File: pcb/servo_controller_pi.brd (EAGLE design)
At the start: 56 parts, among them IC1 PIC18F452, IC2 LM2936MP-3.0, IC3 MAX4173FESA+, Q1 10Mhz

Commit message: Raspberry Pi
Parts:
- removed PW: TL36PO, switch:TL3XPO
- added C10, C11: (no value), rcl:C0805
- added C12: 10uf, rcl:C1206
- added C13: 100nf, rcl:C1206
- added D4: 3V3, diode:SOT23
- added D5: MBRA340T3, diode:SMA
- added GY-27: (no value), con-lstb:MA05-1
- added IC4: LM2936MP-3.3, national-semiconductor:SOT223
- added IC5: 4512D, 45xx:SO16
- added IN, OUT: (no value), con-wago-500:W237-102
- added LED-STRIP: (no value), con-lstb:MA04-1
- added Q2: BUZ10, transistor-fet:TO220
- added R8: (no value), rcl:M0805
- added RN1: (no value), resistor-sil:SIL9
- added SV1, SV2: (no value), con-lstb:MA08-1W
- D2: value 5v1 -> 3V3
- IC2: value LM2936MP-3.0 -> LM2936MP-5.0
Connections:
- removed net N$15: PW.2, X1.2
- new net +15V: IN.1, OUT.1
- new net +3V3: D5.C, U$3.1, U$3.17
- new net ADDRA: IC5.11
- new net ADDRB: IC5.12
- new net ADDRC: IC5.13
- new net CO: LED-STRIP.2
- new net DO: LED-STRIP.3
- new net N$26: IC5.6, RN1.7, SV2.6
- new net N$28: IC5.5, RN1.6, SV2.8
- new net N$29: IC5.4, RN1.5, SV1.2
- new net N$30: IC5.3, RN1.4, SV1.4
- new net N$31: IC5.2, RN1.3, SV1.6
- new net N$33: IC5.1, RN1.2, SV1.8
- new net N$34: IC5.7, RN1.8, SV2.4
- new net N$35: IC5.9, RN1.9, SV2.2
- new net N$36: OUT.2, Q2.2
- new net N$38: C12.1, D5.A, IC4.3
- new net OUT: D4.3, IC5.14
- new net POUT: Q2.1, R8.2
- new net SCL: GY-27.4
- new net SDA: GY-27.3
- net +5V: now also C10.1, C11.1, C13.1, GY-27.5, IC4.1, IC5.16, LED-STRIP.4, SV1.1, SV1.3, SV1.5, SV1.7, SV2.1, SV2.3, SV2.5, SV2.7, U$3.2, U$3.4
- net VDD: now also X1.2; no longer PW.1
- net VSS: now also C10.2, C11.2, C12.2, C13.2, D4.1, GY-27.1, IC4.2, IC4.4, IC5.10, IC5.15, IC5.8, IN.2, LED-STRIP.1, Q2.3, R8.1, RN1.1, U$3.14, U$3.20, U$3.25, U$3.6, U$3.9
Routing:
- net LED0: track 71.1 -> 0.00 mm, vias 1 -> 0
- net VSS: track 195.0 -> 142.9 mm
- net LED1: track 66.0 -> 15.2 mm, vias 2 -> 1
- net SWITCH0: track 72.0 -> 22.1 mm
- net SWITCH1: track 58.3 -> 10.2 mm
- net RX_FROM_ARDUINO: track 29.2 -> 0.27 mm
- net TX_FROM_ARDUINO: track 27.5 -> 0.00 mm
- net VDD: track 144.1 -> 134.6 mm
- net N$15: track 7.23 -> 0.00 mm
- net OPTION0: track 3.07 -> 0.00 mm
- net OPTION3: track 3.07 -> 0.00 mm

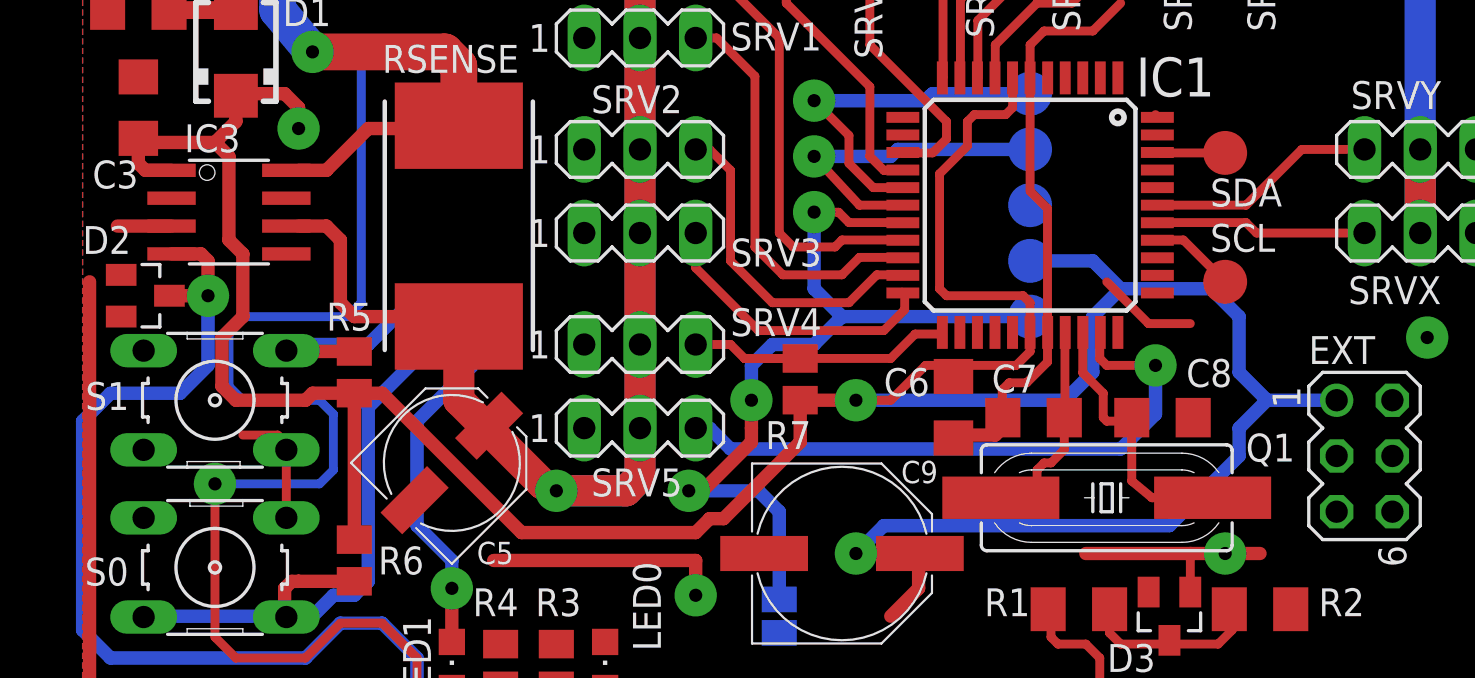
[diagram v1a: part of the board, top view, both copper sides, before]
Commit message: Raspberry Pi pcb version
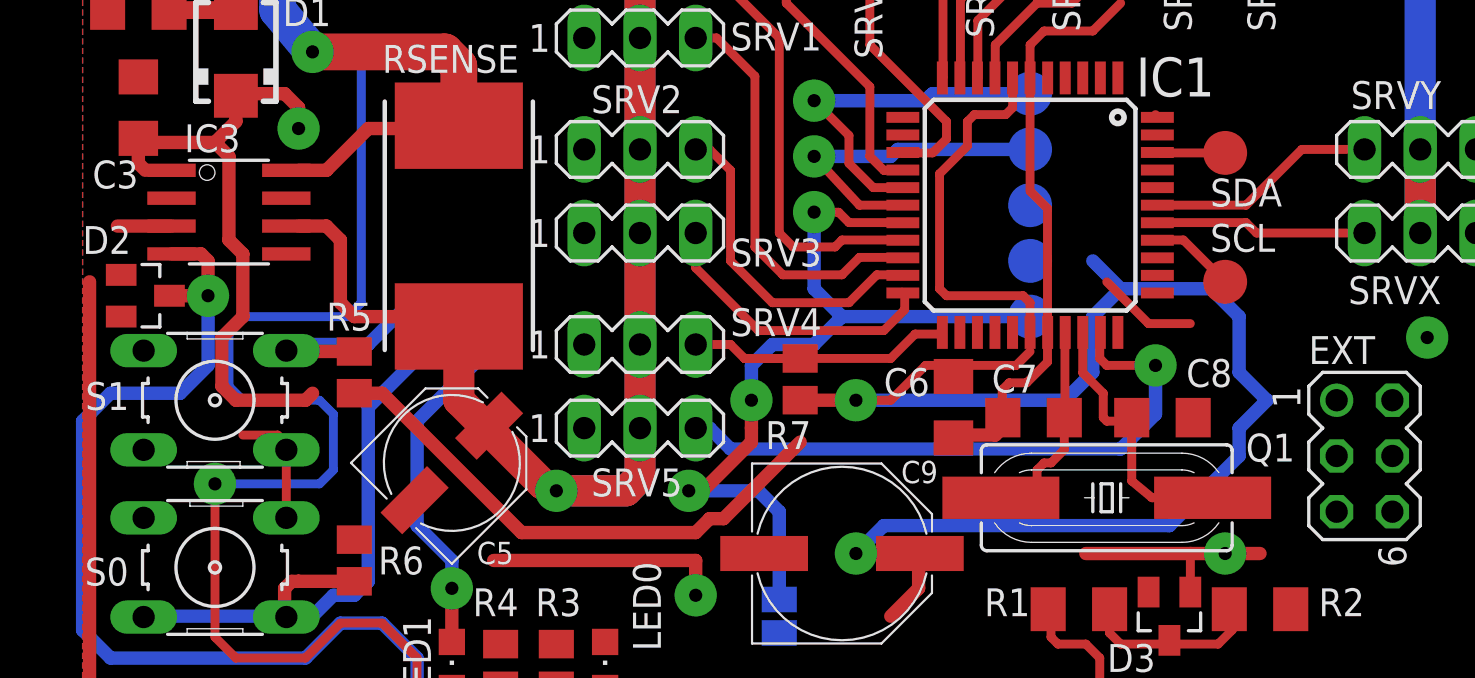
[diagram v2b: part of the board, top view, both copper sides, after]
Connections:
- net +3V3: now also C10.1, C11.1, C3.1, C6.1, EXT.1, GY-27.5, IC1.28, IC1.7, IC3.1, IC5.16, LED-STRIP.4, R5.2, R6.2, R7.2, SV1.1, SV1.3, SV1.5, SV1.7, SV2.1, SV2.3, SV2.5, SV2.7, VDD.TP; no longer U$3.17
- net +5V: no longer C10.1, C11.1, C3.1, C6.1, EXT.1, GY-27.5, IC1.28, IC1.7, IC3.1, IC5.16, LED-STRIP.4, R5.2, R6.2, R7.2, SV1.1, SV1.3, SV1.5, SV1.7, SV2.1, SV2.3, SV2.5, SV2.7, U$3.4, VDD.TP
- net LIPO_VOLTAGE: now also IC1.24
- net SERVO_CURRENT: now also IC1.25
- net VSS: no longer U$3.14, U$3.20, U$3.25, U$3.9
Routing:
- net +5V: track 160.0 -> 97.4 mm
- net +3V3: track 0.00 -> 42.9 mm

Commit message: Schema Pi
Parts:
- removed EXT: (no value), con-lstb:MA03-2
- moved D1 40.5 mm to (35.6, 61.0)
- moved IC2 26.4 mm to (26.7, 61.3)
- moved C1 19.2 mm to (16.8, 61.6)
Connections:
- removed net N$16: SJ1.2
- removed net OPTION0: EXT.3
- removed net OPTION1: EXT.5
- removed net OPTION2: EXT.6
- removed net OPTION3: EXT.4
- removed net RX_FROM_ARDUINO: IC1.44
- removed net SWITCH0: R6.1, S0.1
- removed net SWITCH1: R5.1, S1.2
- removed net TX_FROM_ARDUINO: IC1.1
- new net RX_PI: IC1.44, U$3.10
- new net SO: U$3.23
- new net SW0: R6.1, S0.1, U$3.16
- new net SW1: R5.1, S1.2, U$3.18
- new net TX_PI: IC1.1, U$3.8
- net +3V3: no longer EXT.1, LED-STRIP.4
- net +5V: now also LED-STRIP.4
- net ADDRA: now also U$3.22
- net ADDRB: now also U$3.24
- net ADDRC: now also U$3.26
- net DO: now also U$3.19
- net LED0: now also U$3.7
- net LED1: now also U$3.11
- net OUT: now also U$3.12
- net POUT: now also U$3.15
- net SCL: now also U$3.5
- net SDA: now also U$3.3
- net VSS: no longer EXT.2
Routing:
- net VDD: track 134.6 -> 58.9 mm, vias 2 -> 1
- net SERVO_CURRENT: track 80.9 -> 6.04 mm
- net +5V: track 97.4 -> 69.9 mm, vias 3 -> 2
- net SWITCH0: track 22.1 -> 0.00 mm
- net SW0: track 0.00 -> 22.1 mm
- net SWITCH1: track 10.2 -> 0.00 mm
- net SW1: track 0.00 -> 9.78 mm
- net N$20: track 9.11 -> 0.00 mm

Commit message: Raspberry Pi PCB
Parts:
- moved D2 93.7 mm to (87.9, 61.9)
- moved IC3 92.7 mm to (86.7, 72.7)
- moved C3 90.3 mm to (85.7, 66.7)
- moved RSENSE 88.1 mm to (95.2, 66.4)
- moved S0 72.8 mm to (56.2, 61.6)
- moved C9 72.3 mm to (72.7, 70.5)
- moved S1 71.9 mm to (55.6, 68.6)
- moved D3 69.2 mm to (37.5, 73.3)
- moved R6 69.0 mm to (57.5, 61.3)
- moved R5 68.9 mm to (58.1, 69.2)
- moved R1 68.1 mm to (32.7, 72.4)
- moved R2 67.9 mm to (42.2, 72.4)
- moved SJ1 66.8 mm to (22.9, 71.4)
- moved LED0 66.0 mm to (12.4, 67.9)
- moved LED1 66.0 mm to (5.40, 67.9)
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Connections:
- net UC_RESET: no longer SJ1.1
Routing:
- net VDD: track 58.9 -> 0.00 mm, vias 1 -> 0
- net +5V: track 69.9 -> 11.4 mm, vias 2 -> 0
- net N$6: track 28.1 -> 54.2 mm
- net +3V3: track 42.9 -> 17.6 mm
- net SW0: track 22.1 -> 0.00 mm
- net N$5: track 14.5 -> 35.0 mm
- net N$4: track 13.5 -> 28.9 mm
- net LED1: track 15.2 -> 0.00 mm, vias 1 -> 0
- net N$10: track 17.6 -> 32.5 mm
- net VEE: track 170.4 -> 155.9 mm, vias 1 -> 0
- net N$12: track 11.0 -> 25.1 mm
- net N$13: track 8.91 -> 22.9 mm
- net N$11: track 14.7 -> 28.7 mm
- net N$32: track 15.1 -> 26.3 mm
- net N$3: track 15.3 -> 26.2 mm
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
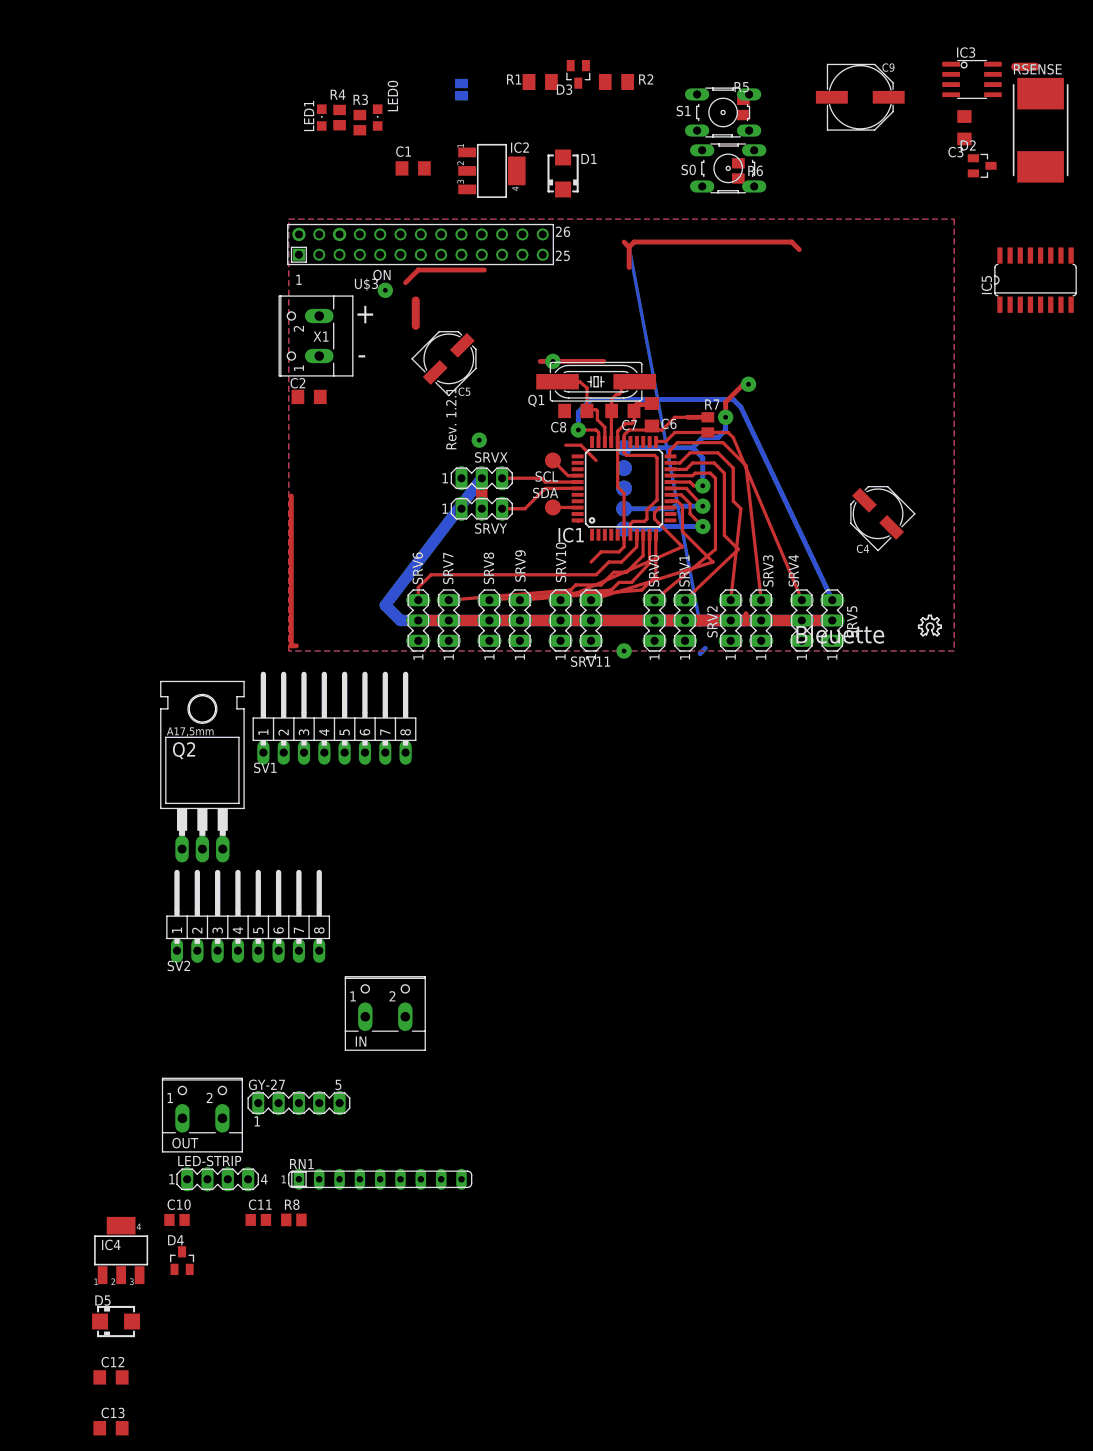
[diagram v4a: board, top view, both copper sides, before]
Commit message: Sensor board milling + Raspberry Pi update
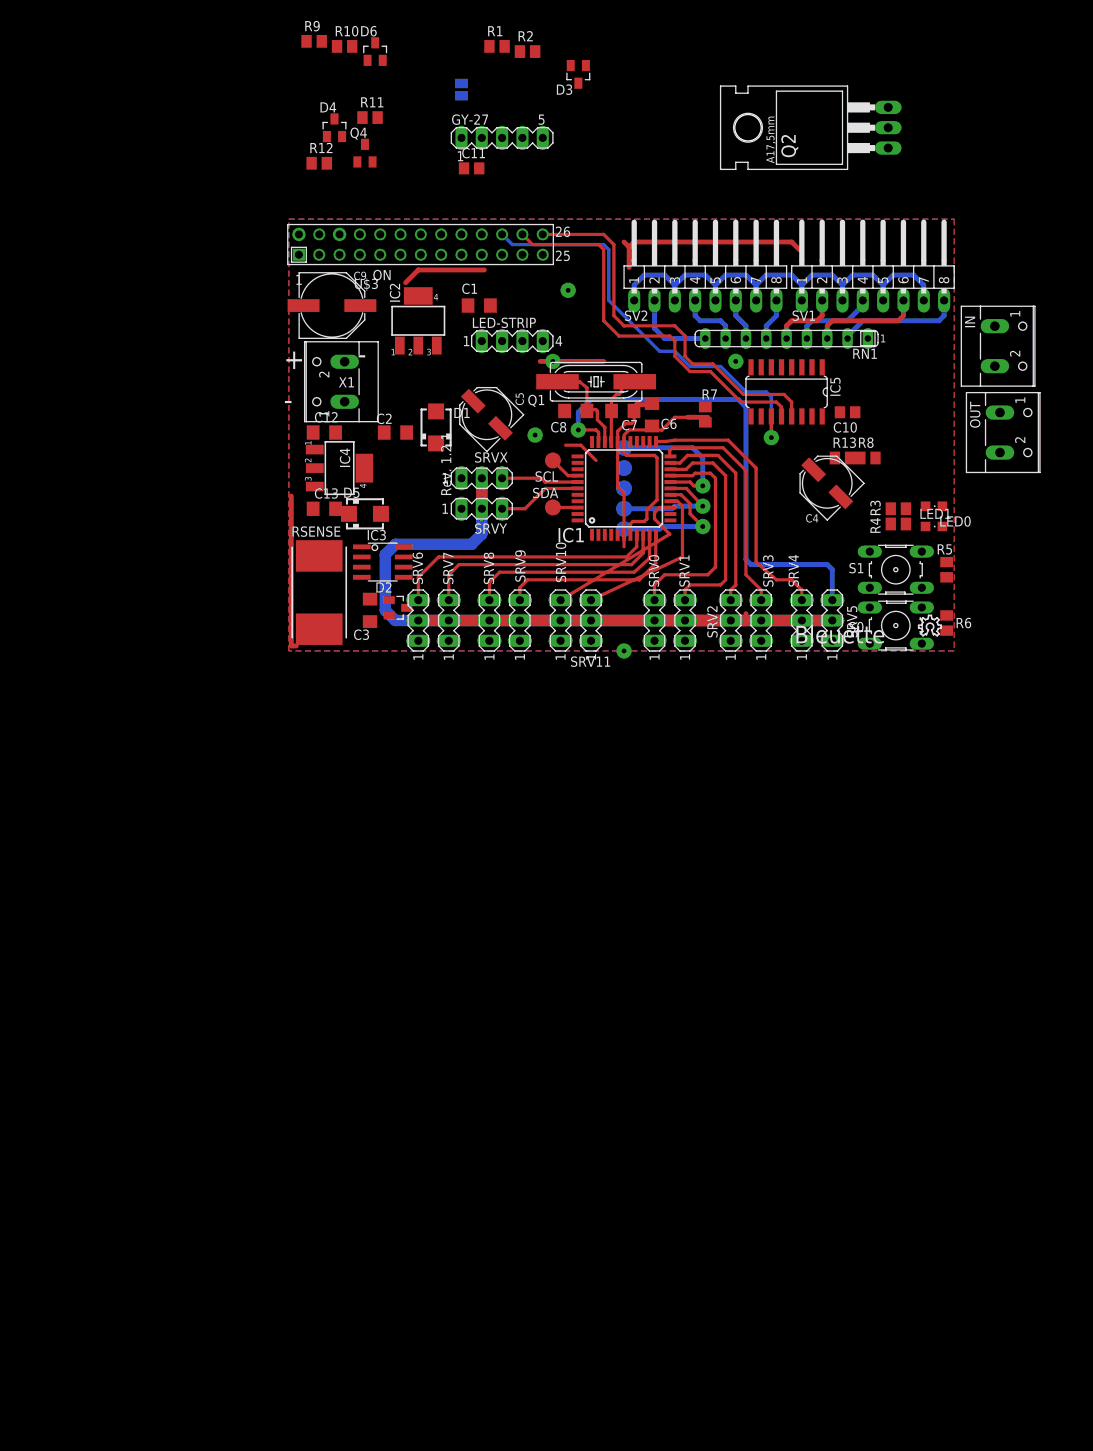
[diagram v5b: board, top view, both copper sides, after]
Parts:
- added D6: 3V3, diode:SOT23
- added Q4: BC848ALT1SMD, transistor-npn:SOT23
- added R10: 2k2, rcl:M0805
- added R11, R12, R13: 1k, rcl:M0805
- added R9: 3k3, rcl:M0805
- D2: value 3V3 -> 5V1
- R1, R2: device rcl:M1206 -> rcl:M0805
- moved D4 142.9 mm to (6.99, 66.7)
- moved C11 134.1 mm to (24.1, 61.6)
- moved OUT 131.6 mm to (91.4, 28.6), turned to 270 degrees
- moved C10 131.2 mm to (71.1, 31.1), turned to 180 degrees
- moved GY-27 123.3 mm to (27.9, 65.4)
- moved C12 121.1 mm to (5.71, 28.6)
- moved R8 119.3 mm to (73.7, 25.4)
- moved C13 118.0 mm to (5.71, 19.1)
- moved RN1 116.7 mm to (63.5, 40.3), turned to 180 degrees
- moved Q2 115.4 mm to (69.8, 66.7), turned to 90 degrees
- moved IN 113.2 mm to (90.8, 39.4), turned to 270 degrees
- moved LED-STRIP 111.1 mm to (29.2, 40.0)
- moved RSENSE 107.1 mm to (5.08, 8.57)
- moved D5 105.7 mm to (10.8, 18.4)
- moved IC4 101.5 mm to (7.62, 24.1), turned to 270 degrees
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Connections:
- new net N$15: IC1.1, Q4.2, R11.1
- new net N$16: IC1.44, R10.2
- new net N$21: D4.3, Q4.1, R12.1
- new net N$37: IC5.14, R13.2
- net +3V3: no longer C3.1, C6.1, IC1.28, IC1.7, IC3.1, R7.2, VDD.TP
- net +5V: now also C3.1, C6.1, IC1.28, IC1.7, IC3.1, Q4.3, R7.2, VDD.TP
- net OUT: now also R13.1; no longer D4.3, IC5.14
- net RX_PI: now also D6.3, R10.1, R9.2; no longer IC1.44
- net TX_PI: now also R12.2; no longer IC1.1
- net VSS: now also D6.1, R11.2, R9.1
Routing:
- net VSS: track 148.6 -> 89.8 mm, vias 4 -> 5
- net ADDRA: track 0.00 -> 53.5 mm, vias 0 -> 1
- net ADDRB: track 0.00 -> 48.8 mm
- net ADDRC: track 0.00 -> 48.3 mm
- net +3V3: track 17.6 -> 58.8 mm
- net +5V: track 11.4 -> 29.0 mm
- net N$33: track 0.00 -> 15.3 mm
- net N$31: track 0.00 -> 14.2 mm
- net UC_RESET: track 30.4 -> 18.1 mm, vias 3 -> 1
- net N$35: track 0.00 -> 10.4 mm
- net N$30: track 0.00 -> 10.3 mm
- net N$29: track 0.00 -> 8.46 mm
- net N$6: track 54.2 -> 62.3 mm
- net N$34: track 0.00 -> 7.83 mm
- net VEE: track 155.9 -> 162.8 mm
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
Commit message: RaspPi Board
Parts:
- added IC7: LM358D, linear:SO08
- C3, C6, C7, C8: device rcl:C1206 -> rcl:C0805
- moved C6 17.9 mm to (40.6, 14.0), turned to 0 degrees
- moved C5 16.0 mm to (17.8, 17.1), turned to 270 degrees
- moved C1 12.6 mm to (15.9, 35.9)
- moved IC3 11.9 mm to (4.45, 4.13)
- moved C3 9.03 mm to (2.54, 7.94), turned to 0 degrees
- moved D2 8.94 mm to (6.35, 9.21)
- moved RSENSE 7.05 mm to (12.1, 7.62)
- moved R13 6.98 mm to (70.5, 32.4), turned to 180 degrees
- moved D5 6.07 mm to (14.9, 22.9)
- moved C10 4.51 mm to (67.6, 28.3)
- moved R7 2.48 mm to (51.4, 29.2)
- moved GY-27 1.42 mm to (26.7, 66.0)
- moved C8 0.97 mm to (38.1, 31.4)
- moved C7 0.81 mm to (42.2, 31.4)
- moved LED-STRIP 0.71 mm to (29.8, 39.7)
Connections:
- new net V+: IC7.8
- new net V-: IC7.4
- net +5V: no longer U$3.2
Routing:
- net OUT: track 0.00 -> 76.6 mm, vias 0 -> 1
- net SERVO_CURRENT: track 0.00 -> 53.7 mm, vias 0 -> 1
- net VSS: track 89.8 -> 38.1 mm
- net +5V: track 29.0 -> 17.6 mm
- net N$6: track 62.3 -> 55.6 mm
- net N$34: track 7.83 -> 14.4 mm
- net N$33: track 15.3 -> 21.5 mm
- net N$37: track 0.00 -> 5.75 mm
- net N$26: track 5.29 -> 10.8 mm
- net N$28: track 5.29 -> 9.67 mm
- net N$29: track 8.46 -> 12.3 mm
- net N$30: track 10.3 -> 14.1 mm
- net N$31: track 14.2 -> 17.9 mm
- net LIPO_VOLTAGE: track 0.00 -> 3.10 mm
- net ADDRA: track 53.5 -> 56.4 mm
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
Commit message: Rapsberry Pi board
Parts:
- removed D4: 3V3, diode:SOT23
- removed GY-27: (no value), con-lstb:MA05-1
- removed LED0, LED1: (no value), led:CHIPLED_0805
- removed R3, R4: 1k, rcl:M0805
- removed R5, R6: 2.2k, rcl:M0805
- removed S0, S1: (no value), switch-omron:B3F-10XX
- added LED2: (no value), led:CHIPLED_0805
- added R14: 1k, rcl:M0805
- added SV3: (no value), con-lstb:MA04-2
- added U$4: GY-27, gy-27:GY-27
- moved IC7 108.2 mm to (79.1, 16.8)
- moved R9 64.3 mm to (29.5, 18.3)
- moved R10 64.0 mm to (34.0, 18.3)
- moved C11 63.0 mm to (66.0, 14.6)
- moved D6 58.9 mm to (31.8, 20.6), turned to 180 degrees
- moved R11 55.1 mm to (30.5, 16.2), turned to 180 degrees
- moved Q4 54.1 mm to (35.9, 15.6), turned to 90 degrees
- moved LED-STRIP 47.3 mm to (72.1, 18.4), turned to 90 degrees
- moved D3 42.8 mm to (24.1, 32.7), turned to 270 degrees
- moved R1 41.9 mm to (22.2, 35.2), turned to 180 degrees
- moved R2 41.3 mm to (26.0, 35.2), turned to 180 degrees
- moved C4 26.8 mm to (48.3, 4.76), turned to 90 degrees
- moved SJ1 18.4 mm to (35.9, 58.4), turned to 180 degrees
- moved R12 16.2 mm to (12.7, 47.9), turned to 180 degrees
- moved SRV1 7.62 mm to (58.4, 5.08)
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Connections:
- net DO renamed DI
- removed net CO: LED-STRIP.2
- removed net LED0: LED0.C, U$3.7
- removed net LED1: LED1.C, U$3.11
- removed net N$7: LED0.A, R3.2
- removed net N$8: LED1.A, R4.2
- removed net SO: U$3.23
- removed net SW0: R6.1, S0.1, U$3.16
- removed net SW1: R5.1, S1.2, U$3.18
- new net N$39: LED2.A, R14.2
- new net OPTION0: SV3.3, U$3.7
- new net OPTION1: SV3.4, U$3.11
- new net OPTION2: SV3.5, U$3.16
- new net OPTION3: SV3.6, U$3.18
- new net SI: LED-STRIP.2, U$3.23
- net +3V3: now also LED2.C, SV3.1, U$4.VCC; no longer GY-27.5, R5.2, R6.2
- net N$21: no longer D4.3
- net SCL: now also SV3.7, U$4.SCL; no longer GY-27.4
- net SDA: now also SV3.8, U$4.SDA; no longer GY-27.3
- net VSS: now also R14.1, SV3.2, U$4.GND; no longer D4.1, GY-27.1, R3.1, R4.1, S0.3, S0.4, S1.3, S1.4
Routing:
- net VEE: track 161.9 -> 196.1 mm
- net VDD: track 0.00 -> 19.3 mm
- net SERVO_CURRENT: track 53.7 -> 70.6 mm, vias 1 -> 0
- net N$33: track 21.5 -> 6.47 mm
- net VSS: track 38.1 -> 49.8 mm, vias 5 -> 6
- net +5V: track 17.6 -> 28.9 mm
- net N$5: track 35.0 -> 45.9 mm
- net N$4: track 27.7 -> 36.0 mm
- net N$15: track 0.00 -> 8.18 mm
- net N$24: track 10.5 -> 2.46 mm
- net N$6: track 55.6 -> 63.2 mm
- net N$19: track 9.64 -> 3.13 mm
- net N$3: track 24.5 -> 31.0 mm
- net N$14: track 24.5 -> 18.0 mm
- net N$1: track 27.6 -> 22.2 mm
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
